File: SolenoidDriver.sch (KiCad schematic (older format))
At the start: 8 parts

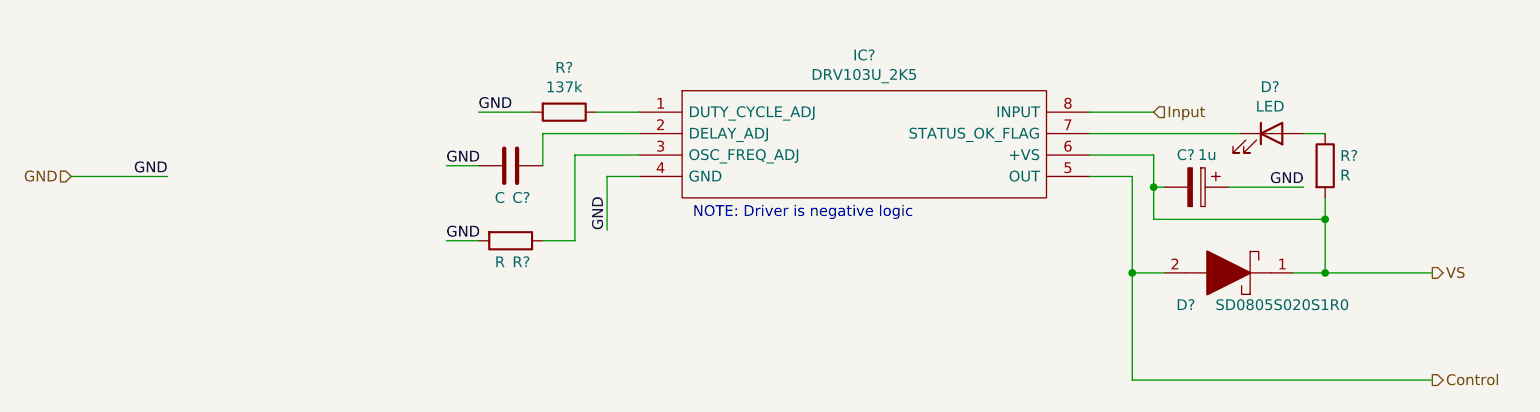
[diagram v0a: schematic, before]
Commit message: Schematic Updates
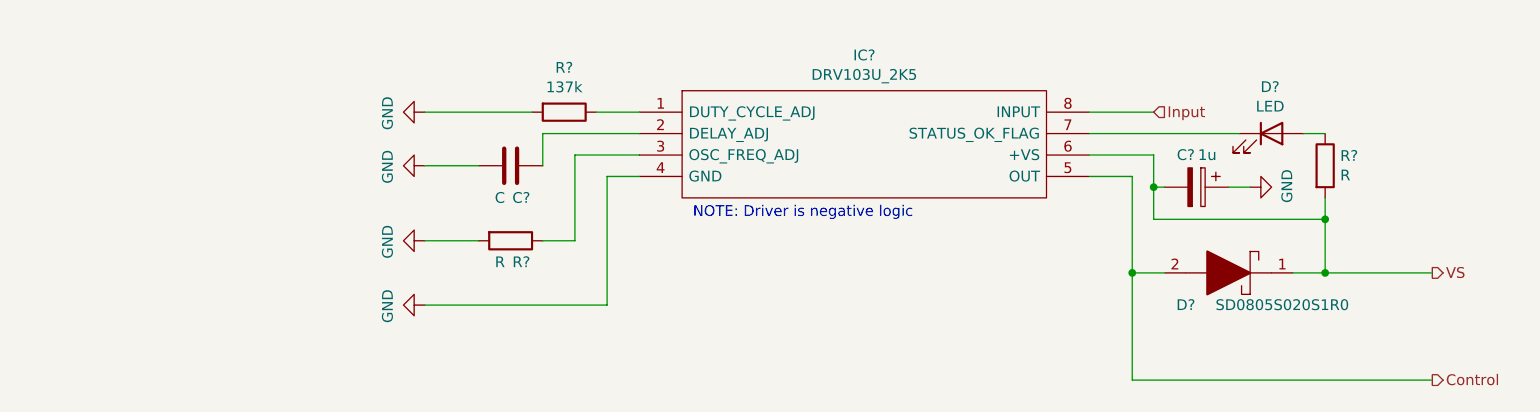
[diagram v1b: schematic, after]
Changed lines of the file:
@@
 Comment4 ""
 $EndDescr
-Text HLabel 1900 2300 0    50   Input ~ 0
-GND
-Wire Wire Line
-	1900 2300 2350 2300
-Text Label 2350 2300 2    50   ~ 0
-GND
-Wire Wire Line
-	4550 2300 4400 2300
-Wire Wire Line
-	4400 2300 4400 2550
-Text Label 4400 2550 1    50   ~ 0
-GND
 Text HLabel 6950 2000 2    50   Input ~ 0
 Input
@@
 Wire Wire Line
 	4350 2000 4550 2000
-Wire Wire Line
-	4050 2000 3800 2000
-Text Label 3800 2000 0    50   ~ 0
-GND
 $Comp
 L Device:C C?
@@
 	4100 2100 4100 2250
 Wire Wire Line
-	4100 2100 4550 2100
-Wire Wire Line
-	3800 2250 3650 2250
-Text Label 3650 2600 0    50   ~ 0
-GND
-Wire Wire Line
 	4250 2200 4250 2600
 Wire Wire Line
@@
 	0    1    1    0
 $EndComp
-Wire Wire Line
-	3800 2600 3650 2600
-Text Label 3650 2250 0    50   ~ 0
-GND
+$Comp
+L Capstone:SD0805S020S1R0 D?
+U 1 1 6157A8ED
+P 7700 2750
+F 0 "D?" H 8300 2900 50  0000 C CNN
+F 1 "SD0805S020S1R0" H 7850 2900 50  0000 C CNN
+F 2 "DIOM1613X100N" H 8200 2900 50  0001 L CNN
+F 3 "https://componentsearchengine.com/Datasheets/1/SD0805S020S1R0.pdf" H 8200 2800 50  0001 L CNN
+F 4 "AVX - SD0805S020S1R0 - DIODE, SCHOTTKY, 1A, 20V, SOD-323" H 8200 2700 50  0001 L CNN "Description"
+F 5 "1" H 8200 2600 50  0001 L CNN "Height"
+F 6 "AVX" H 8200 2500 50  0001 L CNN "Manufacturer_Name"
+F 7 "SD0805S020S1R0" H 8200 2400 50  0001 L CNN "Manufacturer_Part_Number"
+F 8 "581-SD0805S020S1R0" H 8200 2300 50  0001 L CNN "Mouser Part Number"
+F 9 "https://www.mouser.co.uk/ProductDetail/AVX/SD0805S020S1R0?qs=jCA%252BPfw4LHbpkAoSnwrdjw%3D%3D" H 8200 2200 50  0001 L CNN "Mouser Price/Stock"
+F 10 "SD0805S020S1R0" H 8200 2100 50  0001 L CNN "Arrow Part Number"
+F 11 "https://www.arrow.com/en/products/sd0805s020s1r0/avx?region=nac" H 8200 2000 50  0001 L CNN "Arrow Price/Stock"
+	1    7700 2750
+	-1   0    0    1
+$EndComp
+Wire Wire Line
+	6650 2300 6850 2300
+Wire Wire Line
+	6850 2300 6850 2750
+Wire Wire Line
+	6850 2750 7000 2750
+Wire Wire Line
+	6850 2750 6850 3250
+Connection ~ 6850 2750
+Text HLabel 8250 3250 2    50   Output ~ 0
+Control
+Wire Wire Line
+	6650 2200 6950 2200
+Wire Wire Line
+	6950 2200 6950 2350
+Wire Wire Line
+	6950 2350 7000 2350
+Wire Wire Line
+	6950 2350 6950 2500
+Wire Wire Line
+	6950 2500 7750 2500
+Wire Wire Line
+	7750 2500 7750 2750
+Wire Wire Line
+	7750 2750 7600 2750
+Connection ~ 6950 2350
+$Comp
+L Device:CP C?
+U 1 1 6157E351
+P 7150 2350
+F 0 "C?" V 7000 2300 50  0000 C CNN
+F 1 "1u" V 7000 2400 50  0000 C CNN
+F 2 "" H 7188 2200 50  0001 C CNN
+F 3 "~" H 7150 2350 50  0001 C CNN
+	1    7150 2350
+	0    1    1    0
+$EndComp
+$Comp
+L Device:LED D?
+U 1 1 615819DE
+P 7500 2100
+F 0 "D?" H 7493 2317 50  0000 C CNN
+F 1 "LED" H 7493 2226 50  0000 C CNN
+F 2 "" H 7500 2100 50  0001 C CNN
+F 3 "~" H 7500 2100 50  0001 C CNN
+	1    7500 2100
+	1    0    0    -1
+$EndComp
+$Comp
+L Device:R R?
+U 1 1 6158256B
+P 7750 2250
+F 0 "R?" H 7820 2296 50  0000 L CNN
+F 1 "R" H 7820 2205 50  0000 L CNN
+F 2 "" V 7680 2250 50  0001 C CNN
+F 3 "~" H 7750 2250 50  0001 C CNN
+	1    7750 2250
+	1    0    0    -1
+$EndComp
+Wire Wire Line
+	7750 2500 7750 2400
+Connection ~ 7750 2500
+Wire Wire Line
+	7750 2100 7650 2100
+Wire Wire Line
+	7350 2100 6650 2100
+Wire Wire Line
+	7750 2750 8250 2750
+Connection ~ 7750 2750
+Text HLabel 8250 2750 2    50   Output ~ 0
+VS
+Wire Wire Line
+	6850 3250 8250 3250
+Text Notes 4800 2500 0    50   ~ 0
+NOTE: Driver is negative logic
+$Comp
+L power:GND #PWR?
+U 1 1 6164E047
+P 3550 2600
+F 0 "#PWR?" H 3550 2350 50  0001 C CNN
+F 1 "GND" H 3555 2427 50  0000 C CNN
+F 2 "" H 3550 2600 50  0001 C CNN
+F 3 "" H 3550 2600 50  0001 C CNN
+	1    3550 2600
+	0    1    1    0
+$EndComp
+Wire Wire Line
+	3550 2600 3800 2600
+$Comp
+L power:GND #PWR?
+U 1 1 61651136
+P 3550 2250
+F 0 "#PWR?" H 3550 2000 50  0001 C CNN
+F 1 "GND" H 3555 2077 50  0000 C CNN
+F 2 "" H 3550 2250 50  0001 C CNN
+F 3 "" H 3550 2250 50  0001 C CNN
+	1    3550 2250
+	0    1    1    0
+$EndComp
+$Comp
+L power:GND #PWR?
+U 1 1 616517DF
+P 3550 2000
+F 0 "#PWR?" H 3550 1750 50  0001 C CNN
+F 1 "GND" H 3555 1827 50  0000 C CNN
+F 2 "" H 3550 2000 50  0001 C CNN
+F 3 "" H 3550 2000 50  0001 C CNN
+	1    3550 2000
+	0    1    1    0
+$EndComp
+Wire Wire Line
+	3550 2000 4050 2000
+Wire Wire Line
+	3550 2250 3800 2250
+$Comp
+L power:GND #PWR?
+U 1 1 61652A81
+P 7400 2350
+F 0 "#PWR?" H 7400 2100 50  0001 C CNN
+F 1 "GND" H 7405 2177 50  0000 C CNN
+F 2 "" H 7400 2350 50  0001 C CNN
+F 3 "" H 7400 2350 50  0001 C CNN
+	1    7400 2350
+	0    -1   -1   0
+$EndComp
+Wire Wire Line
+	7300 2350 7400 2350
+Wire Wire Line
+	4550 2300 4400 2300
+Wire Wire Line
+	4250 2200 4550 2200
+Wire Wire Line
+	4100 2100 4550 2100
 $Comp
 L Capstone:DRV103U_2K5 IC?
@@
 	1    0    0    -1
 $EndComp
-Wire Wire Line
-	4250 2200 4550 2200
-$Comp
-L Capstone:SD0805S020S1R0 D?
-U 1 1 6157A8ED
-P 7700 2750
-F 0 "D?" H 8300 2900 50  0000 C CNN
-F 1 "SD0805S020S1R0" H 7850 2900 50  0000 C CNN
-F 2 "DIOM1613X100N" H 8200 2900 50  0001 L CNN
-F 3 "https://componentsearchengine.com/Datasheets/1/SD0805S020S1R0.pdf" H 8200 2800 50  0001 L CNN
-F 4 "AVX - SD0805S020S1R0 - DIODE, SCHOTTKY, 1A, 20V, SOD-323" H 8200 2700 50  0001 L CNN "Description"
-F 5 "1" H 8200 2600 50  0001 L CNN "Height"
-F 6 "AVX" H 8200 2500 50  0001 L CNN "Manufacturer_Name"
-F 7 "SD0805S020S1R0" H 8200 2400 50  0001 L CNN "Manufacturer_Part_Number"
-F 8 "581-SD0805S020S1R0" H 8200 2300 50  0001 L CNN "Mouser Part Number"
-F 9 "https://www.mouser.co.uk/ProductDetail/AVX/SD0805S020S1R0?qs=jCA%252BPfw4LHbpkAoSnwrdjw%3D%3D" H 8200 2200 50  0001 L CNN "Mouser Price/Stock"
-F 10 "SD0805S020S1R0" H 8200 2100 50  0001 L CNN "Arrow Part Number"
-F 11 "https://www.arrow.com/en/products/sd0805s020s1r0/avx?region=nac" H 8200 2000 50  0001 L CNN "Arrow Price/Stock"
-	1    7700 2750
-	-1   0    0    1
-$EndComp
-Wire Wire Line
-	6650 2300 6850 2300
-Wire Wire Line
-	6850 2300 6850 2750
-Wire Wire Line
-	6850 2750 7000 2750
-Wire Wire Line
-	6850 2750 6850 3250
-Connection ~ 6850 2750
-Text HLabel 8250 3250 2    50   Output ~ 0
-Control
-Wire Wire Line
-	6650 2200 6950 2200
-Wire Wire Line
-	6950 2200 6950 2350
-Wire Wire Line
-	6950 2350 7000 2350
-Wire Wire Line
-	7300 2350 7650 2350
-Text Label 7650 2350 2    50   ~ 0
-GND
-Wire Wire Line
-	6950 2350 6950 2500
-Wire Wire Line
-	6950 2500 7750 2500
-Wire Wire Line
-	7750 2500 7750 2750
-Wire Wire Line
-	7750 2750 7600 2750
-Connection ~ 6950 2350
-$Comp
-L Device:CP C?
-U 1 1 6157E351
-P 7150 2350
-F 0 "C?" V 7000 2300 50  0000 C CNN
-F 1 "1u" V 7000 2400 50  0000 C CNN
-F 2 "" H 7188 2200 50  0001 C CNN
-F 3 "~" H 7150 2350 50  0001 C CNN
-	1    7150 2350
-	0    1    1    0
-$EndComp
-$Comp
-L Device:LED D?
-U 1 1 615819DE
-P 7500 2100
-F 0 "D?" H 7493 2317 50  0000 C CNN
-F 1 "LED" H 7493 2226 50  0000 C CNN
-F 2 "" H 7500 2100 50  0001 C CNN
-F 3 "~" H 7500 2100 50  0001 C CNN
-	1    7500 2100
-	1    0    0    -1
-$EndComp
-$Comp
-L Device:R R?
-U 1 1 6158256B
-P 7750 2250
-F 0 "R?" H 7820 2296 50  0000 L CNN
-F 1 "R" H 7820 2205 50  0000 L CNN
-F 2 "" V 7680 2250 50  0001 C CNN
-F 3 "~" H 7750 2250 50  0001 C CNN
-	1    7750 2250
-	1    0    0    -1
-$EndComp
-Wire Wire Line
-	7750 2500 7750 2400
-Connection ~ 7750 2500
-Wire Wire Line
-	7750 2100 7650 2100
-Wire Wire Line
-	7350 2100 6650 2100
-Wire Wire Line
-	7750 2750 8250 2750
-Connection ~ 7750 2750
-Text HLabel 8250 2750 2    50   Output ~ 0
-VS
-Wire Wire Line
-	6850 3250 8250 3250
-Text Notes 4800 2500 0    50   ~ 0
-NOTE: Driver is negative logic
+$Comp
+L power:GND #PWR?
+U 1 1 61654989
+P 3550 2900
+F 0 "#PWR?" H 3550 2650 50  0001 C CNN
+F 1 "GND" H 3555 2727 50  0000 C CNN
+F 2 "" H 3550 2900 50  0001 C CNN
+F 3 "" H 3550 2900 50  0001 C CNN
+	1    3550 2900
+	0    1    1    0
+$EndComp
+Wire Wire Line
+	3550 2900 4400 2900
+Wire Wire Line
+	4400 2900 4400 2300
 $EndSCHEMATC

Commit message: Schematic Updates, still need component values for driver circuit and keypad connector EDA
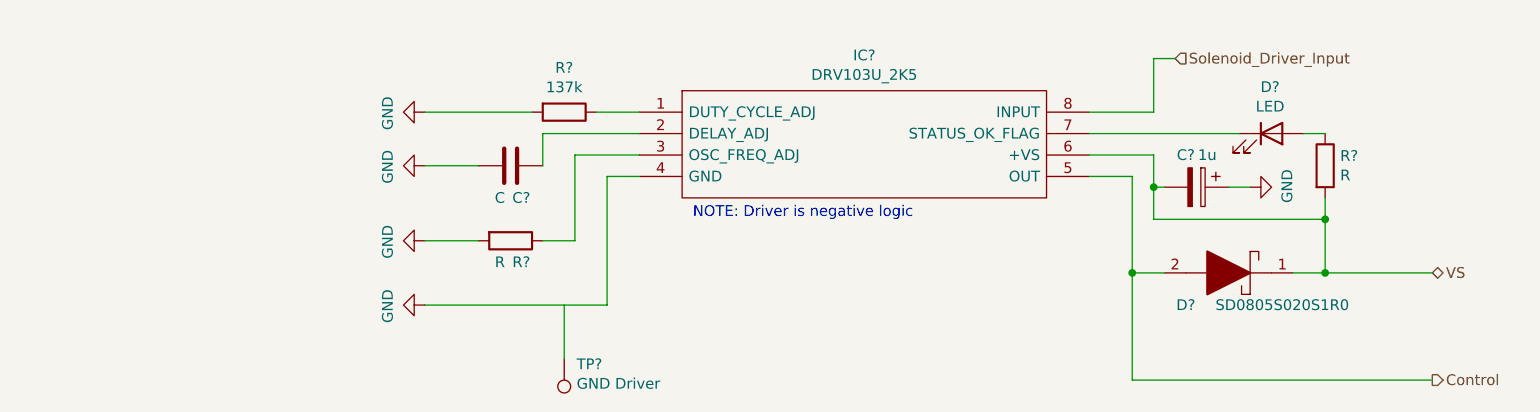
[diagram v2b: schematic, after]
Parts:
- added TP?: GND Driver, symbol Connector:TestPoint
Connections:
- net labels added: Solenoid_Driver_Input
- net labels removed: Input
- wire segments 30 -> 33
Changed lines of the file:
@@
 $Descr A4 11693 8268
 encoding utf-8
-Sheet 3 4
+Sheet 4 4
 Title ""
 Date ""
@@
 Comment4 ""
 $EndDescr
-Text HLabel 6950 2000 2    50   Input ~ 0
-Input
+Text HLabel 7050 1750 2    50   Input ~ 0
+Solenoid_Driver_Input
 Wire Wire Line
 	6950 2000 6650 2000
@@
 	7750 2750 8250 2750
 Connection ~ 7750 2750
-Text HLabel 8250 2750 2    50   Output ~ 0
+Text HLabel 8250 2750 2    50   BiDi ~ 0
 VS
 Wire Wire Line
@@
 Wire Wire Line
 	4400 2900 4400 2300
+Wire Wire Line
+	6950 2000 6950 1750
+Wire Wire Line
+	6950 1750 7050 1750
+$Comp
+L Connector:TestPoint TP?
+U 1 1 6185655C
+P 4200 3150
+AR Path="/61536750/6185655C" Ref="TP?"  Part="1"
+AR Path="/6153F75A/6185655C" Ref="TP?"  Part="1"
+F 0 "TP?" H 4142 3176 50  0000 R CNN
+F 1 "GND Driver" H 4142 3267 50  0000 R CNN
+F 2 "" H 4400 3150 50  0001 C CNN
+F 3 "~" H 4400 3150 50  0001 C CNN
+	1    4200 3150
+	-1   0    0    1
+$EndComp
+Wire Wire Line
+	4200 3150 4200 2900
 $EndSCHEMATC

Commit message: Schematic Updates, still need keypad connector EDA
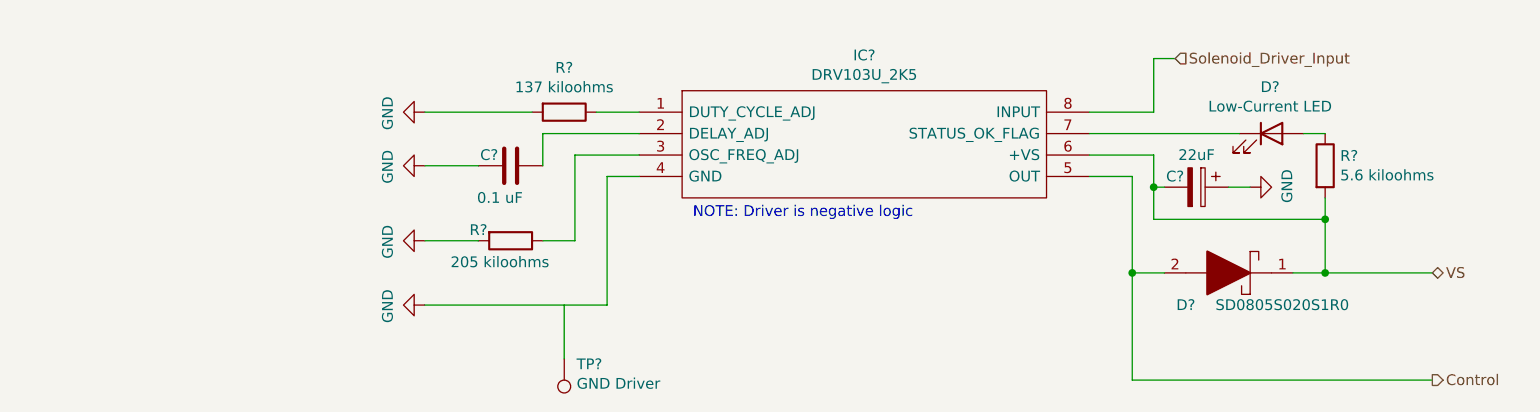
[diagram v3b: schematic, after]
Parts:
- C?: value C -> 0.1 uF
- C?: value 1u -> 22uF
- D?: value LED -> Low-Current LED
- R?: value 137k -> 137 kiloohms
- R?: value R -> 205 kiloohms
- R?: value R -> 5.6 kiloohms
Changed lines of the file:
@@
 P 4200 2000
 F 0 "R?" V 3993 2000 50  0000 C CNN
-F 1 "137k" V 4084 2000 50  0000 C CNN
+F 1 "137 kiloohms" V 4084 2000 50  0000 C CNN
 F 2 "" V 4130 2000 50  0001 C CNN
 F 3 "~" H 4200 2000 50  0001 C CNN
@@
 U 1 1 6157796B
 P 3950 2250
-F 0 "C?" V 4100 2300 50  0000 C CNN
-F 1 "C" V 4100 2200 50  0000 C CNN
+F 0 "C?" V 3900 2150 50  0000 C CNN
+F 1 "0.1 uF" V 4100 2200 50  0000 C CNN
 F 2 "" H 3988 2100 50  0001 C CNN
 F 3 "~" H 3950 2250 50  0001 C CNN
@@
 U 1 1 61579346
 P 3950 2600
-F 0 "R?" V 4050 2650 50  0000 C CNN
-F 1 "R" V 4050 2550 50  0000 C CNN
+F 0 "R?" V 3900 2450 50  0000 C CNN
+F 1 "205 kiloohms" V 4050 2550 50  0000 C CNN
 F 2 "" V 3880 2600 50  0001 C CNN
 F 3 "~" H 3950 2600 50  0001 C CNN
@@
 U 1 1 6157E351
 P 7150 2350
-F 0 "C?" V 7000 2300 50  0000 C CNN
-F 1 "1u" V 7000 2400 50  0000 C CNN
+F 0 "C?" V 7100 2250 50  0000 C CNN
+F 1 "22uF" V 7000 2350 50  0000 C CNN
 F 2 "" H 7188 2200 50  0001 C CNN
 F 3 "~" H 7150 2350 50  0001 C CNN
@@
 P 7500 2100
 F 0 "D?" H 7493 2317 50  0000 C CNN
-F 1 "LED" H 7493 2226 50  0000 C CNN
+F 1 "Low-Current LED" H 7493 2226 50  0000 C CNN
 F 2 "" H 7500 2100 50  0001 C CNN
 F 3 "~" H 7500 2100 50  0001 C CNN
@@
 P 7750 2250
 F 0 "R?" H 7820 2296 50  0000 L CNN
-F 1 "R" H 7820 2205 50  0000 L CNN
+F 1 "5.6 kiloohms" H 7820 2205 50  0000 L CNN
 F 2 "" V 7680 2250 50  0001 C CNN
 F 3 "~" H 7750 2250 50  0001 C CNN

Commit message: Added Generic Keypad Connector, don't know if we can use it or not
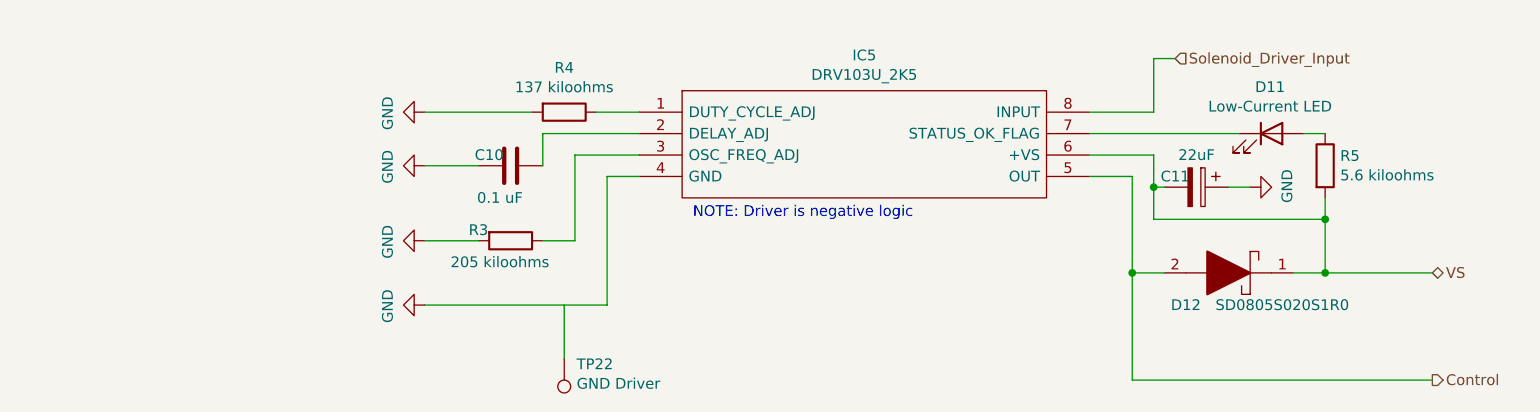
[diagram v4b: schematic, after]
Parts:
- gave numbers to parts that had none: 9
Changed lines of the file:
@@
 	6950 2000 6650 2000
 $Comp
-L Device:R R?
+L Device:R R4
 U 1 1 6157706B
 P 4200 2000
-F 0 "R?" V 3993 2000 50  0000 C CNN
+F 0 "R4" V 3993 2000 50  0000 C CNN
 F 1 "137 kiloohms" V 4084 2000 50  0000 C CNN
 F 2 "" V 4130 2000 50  0001 C CNN
@@
 	4350 2000 4550 2000
 $Comp
-L Device:C C?
+L Device:C C10
 U 1 1 6157796B
 P 3950 2250
-F 0 "C?" V 3900 2150 50  0000 C CNN
+F 0 "C10" V 3900 2150 50  0000 C CNN
 F 1 "0.1 uF" V 4100 2200 50  0000 C CNN
 F 2 "" H 3988 2100 50  0001 C CNN
@@
 	4250 2600 4100 2600
 $Comp
-L Device:R R?
+L Device:R R3
 U 1 1 61579346
 P 3950 2600
-F 0 "R?" V 3900 2450 50  0000 C CNN
+F 0 "R3" V 3900 2450 50  0000 C CNN
 F 1 "205 kiloohms" V 4050 2550 50  0000 C CNN
 F 2 "" V 3880 2600 50  0001 C CNN
@@
 $EndComp
 $Comp
-L Capstone:SD0805S020S1R0 D?
+L Capstone:SD0805S020S1R0 D12
 U 1 1 6157A8ED
 P 7700 2750
-F 0 "D?" H 8300 2900 50  0000 C CNN
+F 0 "D12" H 8300 2900 50  0000 C CNN
 F 1 "SD0805S020S1R0" H 7850 2900 50  0000 C CNN
 F 2 "DIOM1613X100N" H 8200 2900 50  0001 L CNN
@@
 Connection ~ 6950 2350
 $Comp
-L Device:CP C?
+L Device:CP C11
 U 1 1 6157E351
 P 7150 2350
-F 0 "C?" V 7100 2250 50  0000 C CNN
+F 0 "C11" V 7100 2250 50  0000 C CNN
 F 1 "22uF" V 7000 2350 50  0000 C CNN
 F 2 "" H 7188 2200 50  0001 C CNN
@@
 $EndComp
 $Comp
-L Device:LED D?
+L Device:LED D11
 U 1 1 615819DE
 P 7500 2100
-F 0 "D?" H 7493 2317 50  0000 C CNN
+F 0 "D11" H 7493 2317 50  0000 C CNN
 F 1 "Low-Current LED" H 7493 2226 50  0000 C CNN
 F 2 "" H 7500 2100 50  0001 C CNN
@@
 $EndComp
 $Comp
-L Device:R R?
+L Device:R R5
 U 1 1 6158256B
 P 7750 2250
-F 0 "R?" H 7820 2296 50  0000 L CNN
+F 0 "R5" H 7820 2296 50  0000 L CNN
 F 1 "5.6 kiloohms" H 7820 2205 50  0000 L CNN
 F 2 "" V 7680 2250 50  0001 C CNN
@@
 NOTE: Driver is negative logic
 $Comp
-L power:GND #PWR?
+L power:GND #PWR0124
 U 1 1 6164E047
 P 3550 2600
-F 0 "#PWR?" H 3550 2350 50  0001 C CNN
+F 0 "#PWR0124" H 3550 2350 50  0001 C CNN
 F 1 "GND" H 3555 2427 50  0000 C CNN
 F 2 "" H 3550 2600 50  0001 C CNN
@@
 	3550 2600 3800 2600
 $Comp
-L power:GND #PWR?
+L power:GND #PWR0125
 U 1 1 61651136
 P 3550 2250
-F 0 "#PWR?" H 3550 2000 50  0001 C CNN
+F 0 "#PWR0125" H 3550 2000 50  0001 C CNN
 F 1 "GND" H 3555 2077 50  0000 C CNN
 F 2 "" H 3550 2250 50  0001 C CNN
@@
 $EndComp
 $Comp
-L power:GND #PWR?
+L power:GND #PWR0126
 U 1 1 616517DF
 P 3550 2000
-F 0 "#PWR?" H 3550 1750 50  0001 C CNN
+F 0 "#PWR0126" H 3550 1750 50  0001 C CNN
 F 1 "GND" H 3555 1827 50  0000 C CNN
 F 2 "" H 3550 2000 50  0001 C CNN
@@
 	3550 2250 3800 2250
 $Comp
-L power:GND #PWR?
+L power:GND #PWR0127
 U 1 1 61652A81
 P 7400 2350
-F 0 "#PWR?" H 7400 2100 50  0001 C CNN
+F 0 "#PWR0127" H 7400 2100 50  0001 C CNN
 F 1 "GND" H 7405 2177 50  0000 C CNN
 F 2 "" H 7400 2350 50  0001 C CNN
@@
 	4100 2100 4550 2100
 $Comp
-L Capstone:DRV103U_2K5 IC?
+L Capstone:DRV103U_2K5 IC5
 U 1 1 61573BB1
 P 4550 2000
-F 0 "IC?" H 5600 2265 50  0000 C CNN
+F 0 "IC5" H 5600 2265 50  0000 C CNN
 F 1 "DRV103U_2K5" H 5600 2174 50  0000 C CNN
 F 2 "SOIC127P600X175-8N" H 6500 2100 50  0001 L CNN
@@
 $EndComp
 $Comp
-L power:GND #PWR?
+L power:GND #PWR0128
 U 1 1 61654989
 P 3550 2900
-F 0 "#PWR?" H 3550 2650 50  0001 C CNN
+F 0 "#PWR0128" H 3550 2650 50  0001 C CNN
 F 1 "GND" H 3555 2727 50  0000 C CNN
 F 2 "" H 3550 2900 50  0001 C CNN
@@
 P 4200 3150
 AR Path="/61536750/6185655C" Ref="TP?"  Part="1"
-AR Path="/6153F75A/6185655C" Ref="TP?"  Part="1"
-F 0 "TP?" H 4142 3176 50  0000 R CNN
+AR Path="/6153F75A/6185655C" Ref="TP22"  Part="1"
+F 0 "TP22" H 4142 3176 50  0000 R CNN
 F 1 "GND Driver" H 4142 3267 50  0000 R CNN
 F 2 "" H 4400 3150 50  0001 C CNN

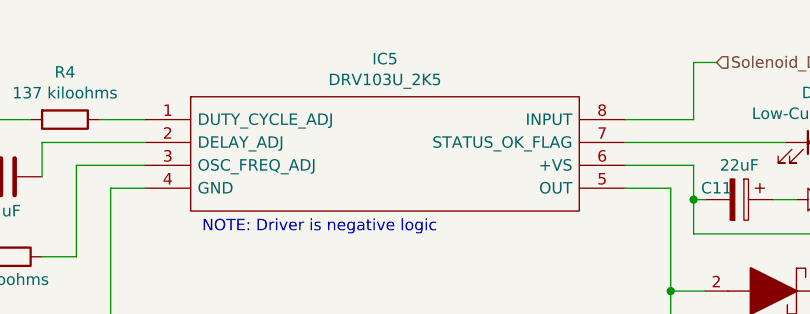
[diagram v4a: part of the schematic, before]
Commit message: Added labels for ease of reading and reorganized a sheet, still have a Generic Keypad Connector, don't know if we can use it or not
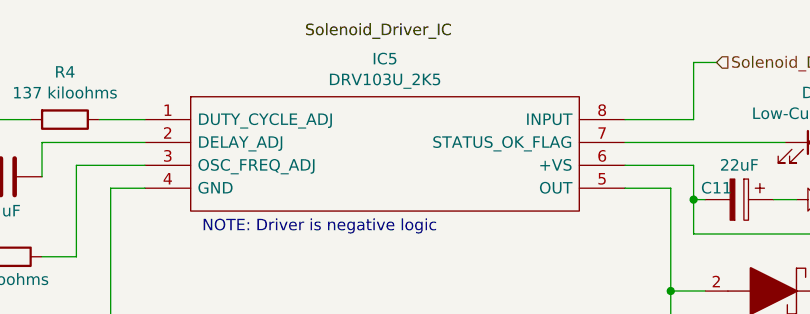
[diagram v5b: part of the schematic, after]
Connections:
- net labels added: Solenoid_Driver_IC
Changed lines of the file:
@@
 Wire Wire Line
 	4200 3150 4200 2900
+Text Label 5250 1650 0    50   ~ 0
+Solenoid_Driver_IC
 $EndSCHEMATC
